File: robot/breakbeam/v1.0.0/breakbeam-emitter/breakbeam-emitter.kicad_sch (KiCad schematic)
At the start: 6 parts, among them J1 Conn_01x03, Q1 RUC002N05T116

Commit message: Mechanical iteration, electrical review
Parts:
- added H1, H2: MountingHole, MountingHole:MountingHole_2.2mm_M2, symbol Mechanical:MountingHole
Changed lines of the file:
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@@
+    )
+  )
+  (symbol (lib_id "Mechanical:MountingHole") (at 160.02 130.81 0) (unit 1)
+    (in_bom yes) (on_board yes) (dnp no) (fields_autoplaced)
+    (property "Reference" "H2" (at 162.56 130.175 0)
+      (effects (font (size 1.27 1.27)) (justify left))
+    )
+    (property "Value" "MountingHole" (at 162.56 132.715 0)
+      (effects (font (size 1.27 1.27)) (justify left))
+    )
+    (property "Footprint" "MountingHole:MountingHole_2.2mm_M2" (at 160.02 130.81 0)
+      (effects (font (size 1.27 1.27)) hide)
+    )
+    (property "Datasheet" "~" (at 160.02 130.81 0)
+      (effects (font (size 1.27 1.27)) hide)
+    )
+    (instances
+      (project "breakbeam-emitter"
+        (path "/b929305a-0bd3-4ebe-83e1-d950a5a5916e"
+          (reference "H2") (unit 1)
+        )
+      )
     )
   )
@@
         )
       )
+    )
+  )
+  (symbol (lib_id "Mechanical:MountingHole") (at 142.24 130.81 0) (unit 1)
+    (in_bom yes) (on_board yes) (dnp no) (fields_autoplaced)
+    (property "Reference" "H1" (at 144.78 130.175 0)
+      (effects (font (size 1.27 1.27)) (justify left))
+    )
+    (property "Value" "MountingHole" (at 144.78 132.715 0)
+      (effects (font (size 1.27 1.27)) (justify left))
+    )
+    (property "Footprint" "MountingHole:MountingHole_2.2mm_M2" (at 142.24 130.81 0)
+      (effects (font (size 1.27 1.27)) hide)
+    )
+    (property "Datasheet" "~" (at 142.24 130.81 0)
+      (effects (font (size 1.27 1.27)) hide)
+    )
+    (instances
+      (project "breakbeam-emitter"
+        (path "/b929305a-0bd3-4ebe-83e1-d950a5a5916e"
+          (reference "H1") (unit 1)
+        )
+      )

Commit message: Ordering changes
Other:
- note added: "I_{f} = (3.3-1.6)/39 = 47.2 mA -> MAX"
- note removed: "I_{f} = (3.3-1.6)/36 = 47.2 mA"
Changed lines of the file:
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@@
     (stroke (width 0) (type default))
   )
-  (text "I_{f} = (3.3-1.6)/36 = 47.2 mA" (at 193.04 95.25 0)
+  (text "I_{f} = (3.3-1.6)/39 = 47.2 mA -> MAX" (at 193.04 95.25 0)
     (effects (font (size 1.27 1.27)) (justify left bottom))
   )

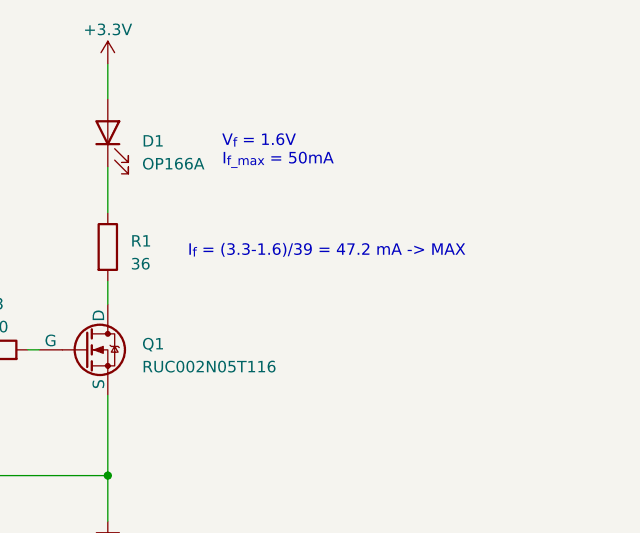
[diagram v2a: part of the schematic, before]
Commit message: Fixed back resistor value
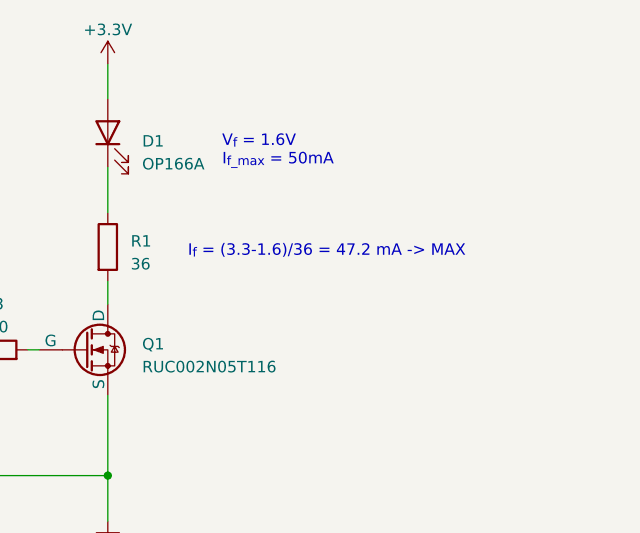
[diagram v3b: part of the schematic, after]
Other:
- note added: "I_{f} = (3.3-1.6)/36 = 47.2 mA -> MAX"
- note removed: "I_{f} = (3.3-1.6)/39 = 47.2 mA -> MAX"
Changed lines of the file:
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@@
     (stroke (width 0) (type default))
   )
-  (text "I_{f} = (3.3-1.6)/39 = 47.2 mA -> MAX" (at 193.04 95.25 0)
+  (text "I_{f} = (3.3-1.6)/36 = 47.2 mA -> MAX" (at 193.04 95.25 0)
     (effects (font (size 1.27 1.27)) (justify left bottom))
   )
